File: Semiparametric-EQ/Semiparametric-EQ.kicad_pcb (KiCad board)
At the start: 2 copper layers, 100 x 100 mm, 52 parts, among them J1 Conn_01x05_Male, J2 Conn_01x02_Male, SW1 Peak/Shelf, U1 NE5532, U2 TL072, U3 NE5532

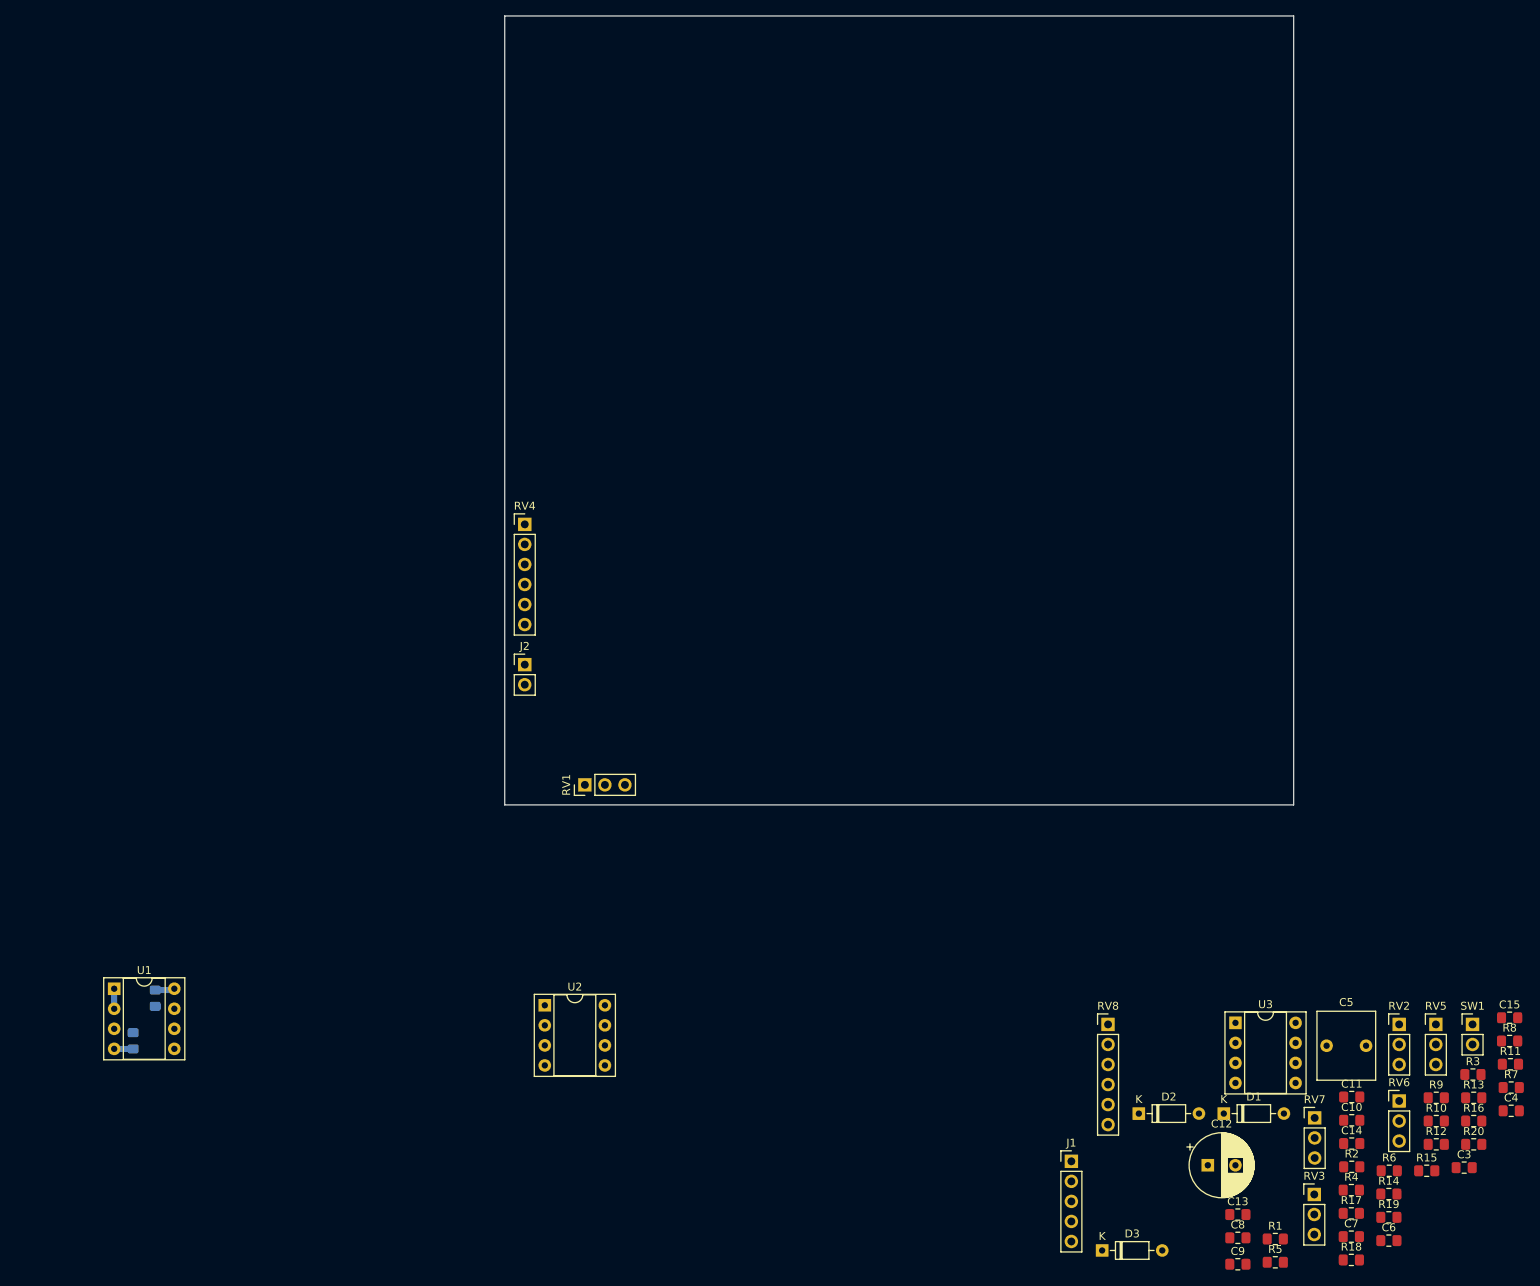
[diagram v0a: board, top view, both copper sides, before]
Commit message: More layout work on the EQ unit
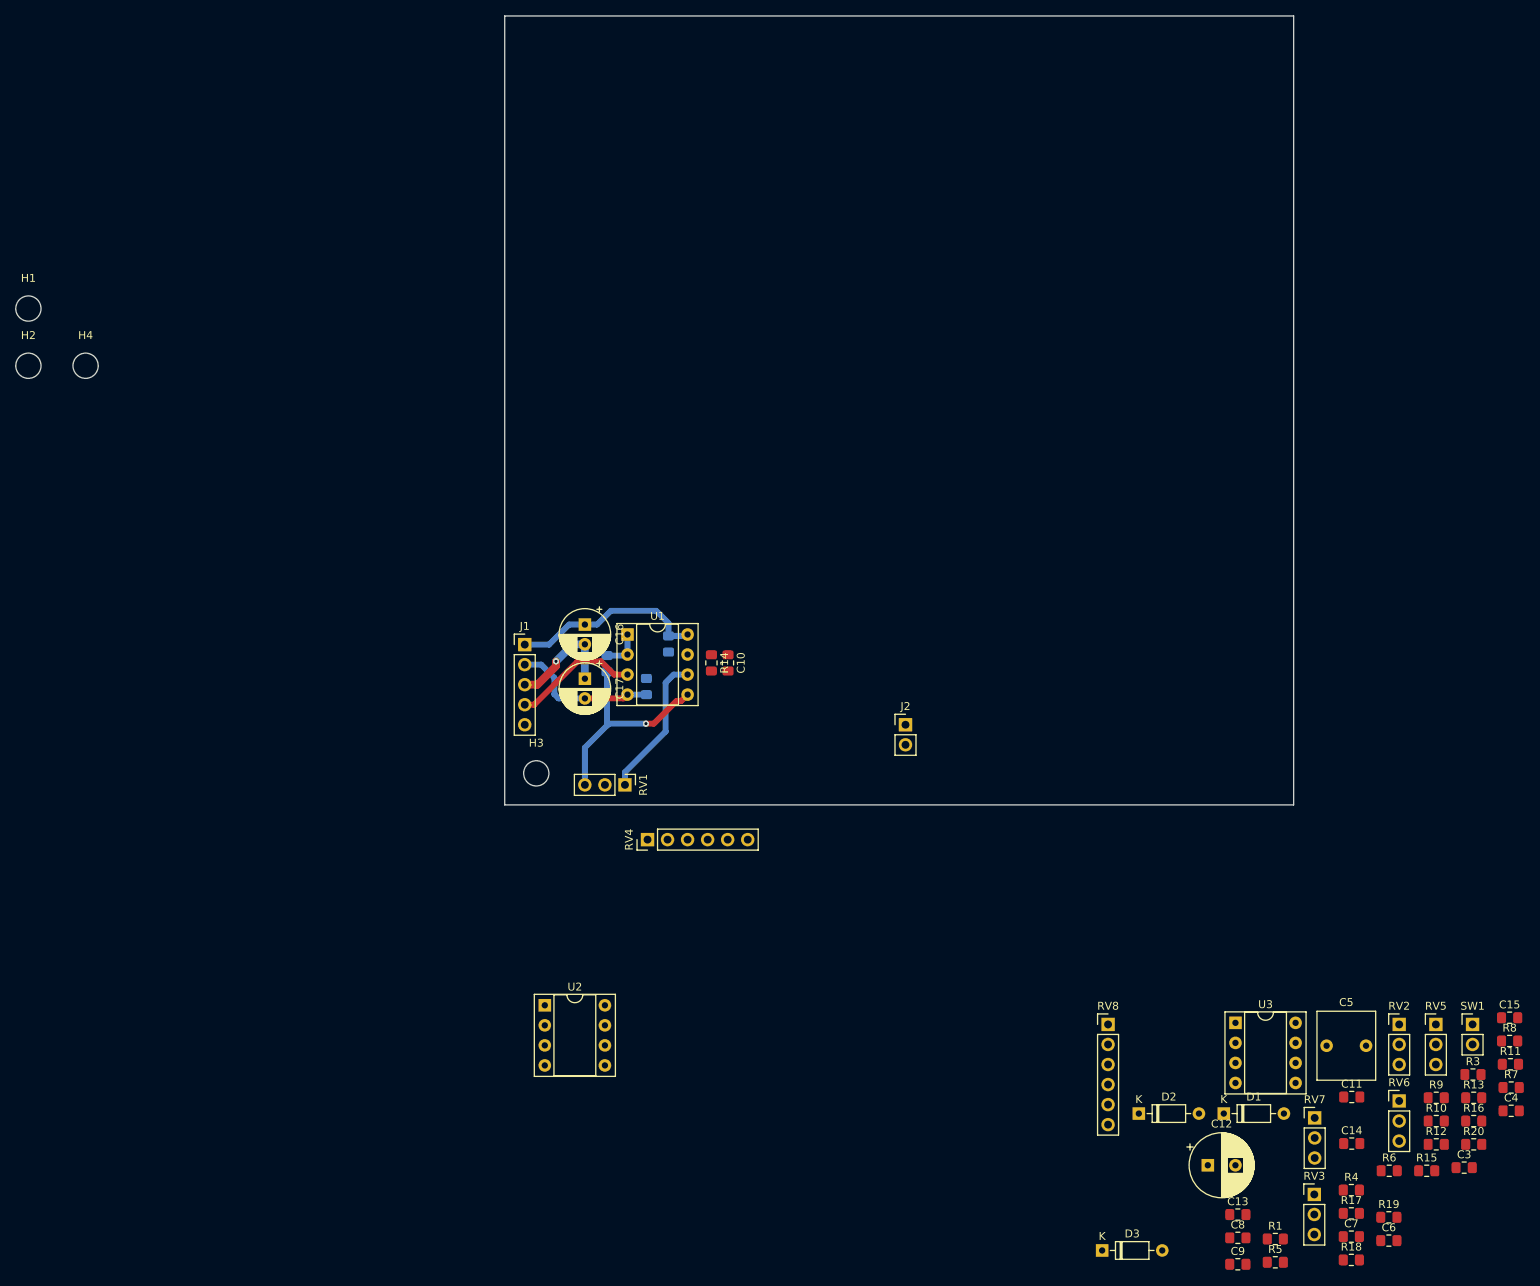
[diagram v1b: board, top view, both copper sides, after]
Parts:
- added C16: 100uF 25V, Capacitor_THT:CP_Radial_D6.3mm_P2.50mm, F.Cu at (10.2, -22.9)
- added C17: 100uF 25V, Capacitor_THT:CP_Radial_D6.3mm_P2.50mm, F.Cu at (10.2, -16.0)
- added H1: MountingHole, MountingHole:MountingHole_3.2mm_M3_ISO7380, F.Cu at (-60.4, -62.9)
- added H2: MountingHole, MountingHole:MountingHole_3.2mm_M3_ISO7380, F.Cu at (-60.4, -55.7)
- added H3: MountingHole, MountingHole:MountingHole_3.2mm_M3_ISO7380, F.Cu at (4.00, -4.00)
- added H4: MountingHole, MountingHole:MountingHole_3.2mm_M3_ISO7380, F.Cu at (-53.1, -55.7)
- R2: moved to B.Cu
- moved R2 113.9 mm to (13.0, -17.9), turned to 90 degrees
- moved R14 109.1 mm to (26.2, -18.0), turned to 270 degrees
- moved C10 98.0 mm to (28.3, -18.0), turned to 270 degrees
- moved J1 95.3 mm to (2.54, -20.3)
- moved C1 79.0 mm to (20.8, -20.4)
- moved C2 79.0 mm to (18.0, -15.0)
- moved U1 79.0 mm to (15.6, -21.6)
- moved J2 48.9 mm to (50.8, -10.2)
- moved RV4 42.9 mm to (18.1, 4.40), turned to 90 degrees
- moved RV1 5.08 mm to (15.2, -2.54), turned to 270 degrees
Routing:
- net Net-(R2-Pad1): track 0.00 -> 27.3 mm, vias 0 -> 1
- net +12V: track 2.49 -> 24.7 mm
- net Net-(C10-Pad2): track 0.00 -> 18.3 mm
- net -12V: track 2.40 -> 18.6 mm
- net IntoEQ: track 0.00 -> 16.0 mm
- net GND: track 0.00 -> 14.5 mm, vias 0 -> 1
- net Net-(R2-Pad2): track 2.54 -> 5.20 mm

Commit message: More layout on EQ
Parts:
- C10, C13, C14, C15, C7, C8, R1, R17, R5, R6: moved to B.Cu
- moved R4 139.9 mm to (-20.7, -7.60)
- moved C12 137.2 mm to (-8.40, -50.8)
- moved H1 125.5 mm to (61.0, -31.0)
- moved H4 125.3 mm to (61.0, -4.00)
- moved R1 124.0 mm to (4.30, -26.5), turned to 180 degrees
- moved C15 115.7 mm to (24.4, -25.8), turned to 270 degrees
- moved C14 108.9 mm to (27.7, -31.3), turned to 270 degrees
- moved RV2 107.6 mm to (10.2, -2.54), turned to 90 degrees
- moved SW1 107.5 mm to (20.3, -5.08)
- moved R8 100.4 mm to (36.9, -13.5)
- moved C7 98.1 mm to (29.7, -5.20)
- moved C5 97.5 mm to (17.7, -14.6), turned to 180 degrees
- moved R5 95.7 mm to (25.8, -5.20), turned to 180 degrees
- moved U3 92.5 mm to (22.2, -32.4)
- moved RV3 90.9 mm to (27.9, -2.54), turned to 90 degrees
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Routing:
- net Net-(C5-Pad2): track 0.00 -> 17.9 mm
- net GND: track 14.5 -> 0.00 mm, vias 1 -> 0
- net Net-(C10-Pad2): track 18.3 -> 30.3 mm
- net Net-(C5-Pad1): track 0.00 -> 10.6 mm
- net Net-(C8-Pad2): track 0.00 -> 7.63 mm
- net Net-(C13-Pad2): track 0.00 -> 7.59 mm
- net Net-(C10-Pad1): track 0.00 -> 5.47 mm
- net +12V: track 24.7 -> 30.0 mm
- net Net-(R17-Pad1): track 0.00 -> 5.09 mm
- net Net-(R6-Pad1): track 0.00 -> 4.33 mm
- net -12V: track 18.6 -> 14.9 mm
- net Net-(C7-Pad2): track 0.00 -> 2.76 mm
- net Net-(R5-Pad2): track 0.00 -> 2.45 mm
- net IntoEQ: track 16.0 -> 18.4 mm, vias 0 -> 1
- net Net-(C7-Pad1): track 0.00 -> 1.85 mm
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- added copper zone on B.Cu, net GND

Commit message: Finished first pass at Eq board
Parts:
- removed C3, C4: 0.1uF, Capacitor_SMD:C_0805_2012Metric_Pad1.15x1.40mm_HandSolder
- added C18: 0.1uF, Capacitor_SMD:C_0805_2012Metric_Pad1.15x1.40mm_HandSolder, B.Cu at (41.1, -22.5)
- added C19: 0.1uF, Capacitor_SMD:C_0805_2012Metric_Pad1.15x1.40mm_HandSolder, B.Cu at (33.7, -15.1)
- C10: moved to F.Cu
- C11, C6, C9, R10, R11, R16, R18, R19, R3, R7, R9: moved to B.Cu
- D1, D2, D3: footprint Diode_THT:D_DO-35_SOD27_P7.62mm_Horizontal -> Diode_SMD:D_SOD-123
- moved R7 120.3 mm to (19.9, -17.9), turned to 90 degrees
- moved C6 119.4 mm to (17.7, -17.9), turned to 270 degrees
- moved R3 108.7 mm to (26.2, -15.8), turned to 270 degrees
- moved R18 104.3 mm to (38.2, -20.4), turned to 90 degrees
- moved R9 102.1 mm to (33.2, -19.7), turned to 270 degrees
- moved R20 97.8 mm to (46.1, -17.7), turned to 270 degrees
- moved R19 96.2 mm to (46.1, -17.7), turned to 90 degrees
- moved D3 94.4 mm to (41.4, -31.5), turned to 270 degrees
- moved R11 94.1 mm to (52.9, -24.5), turned to 90 degrees
- moved R16 90.0 mm to (44.9, -5.00), turned to 180 degrees
- moved R15 89.9 mm to (55.7, -19.5), turned to 270 degrees
- moved R10 89.9 mm to (39.0, -2.60), turned to 180 degrees
- moved C9 88.2 mm to (53.7, -20.8)
- moved D1 87.9 mm to (38.8, -31.5), turned to 270 degrees
- moved R13 86.1 mm to (58.0, -19.5), turned to 270 degrees
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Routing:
- net FromEq: track 0.00 -> 94.3 mm
- net Net-(D1-Pad2): track 0.00 -> 77.1 mm, vias 0 -> 1
- net +12V: track 30.0 -> 100.1 mm
- net -12V: track 14.9 -> 70.8 mm, vias 0 -> 2
- net Net-(R2-Pad1): track 29.0 -> 76.0 mm, vias 1 -> 3
- net Net-(C10-Pad2): track 30.3 -> 76.8 mm, vias 0 -> 1
- net Net-(R7-Pad2): track 0.00 -> 44.1 mm, vias 0 -> 1
- net Net-(C6-Pad1): track 0.00 -> 37.2 mm, vias 0 -> 2
- net Para: track 0.00 -> 28.1 mm
- net Net-(R4-Pad2): track 0.00 -> 22.8 mm
- net Net-(R10-Pad2): track 0.00 -> 21.7 mm, vias 0 -> 1
- net Net-(C10-Pad1): track 5.47 -> 22.6 mm
- net Net-(C9-Pad2): track 0.00 -> 13.7 mm
- net Net-(R18-Pad1): track 0.00 -> 12.5 mm
- net Overload: track 0.00 -> 11.5 mm
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
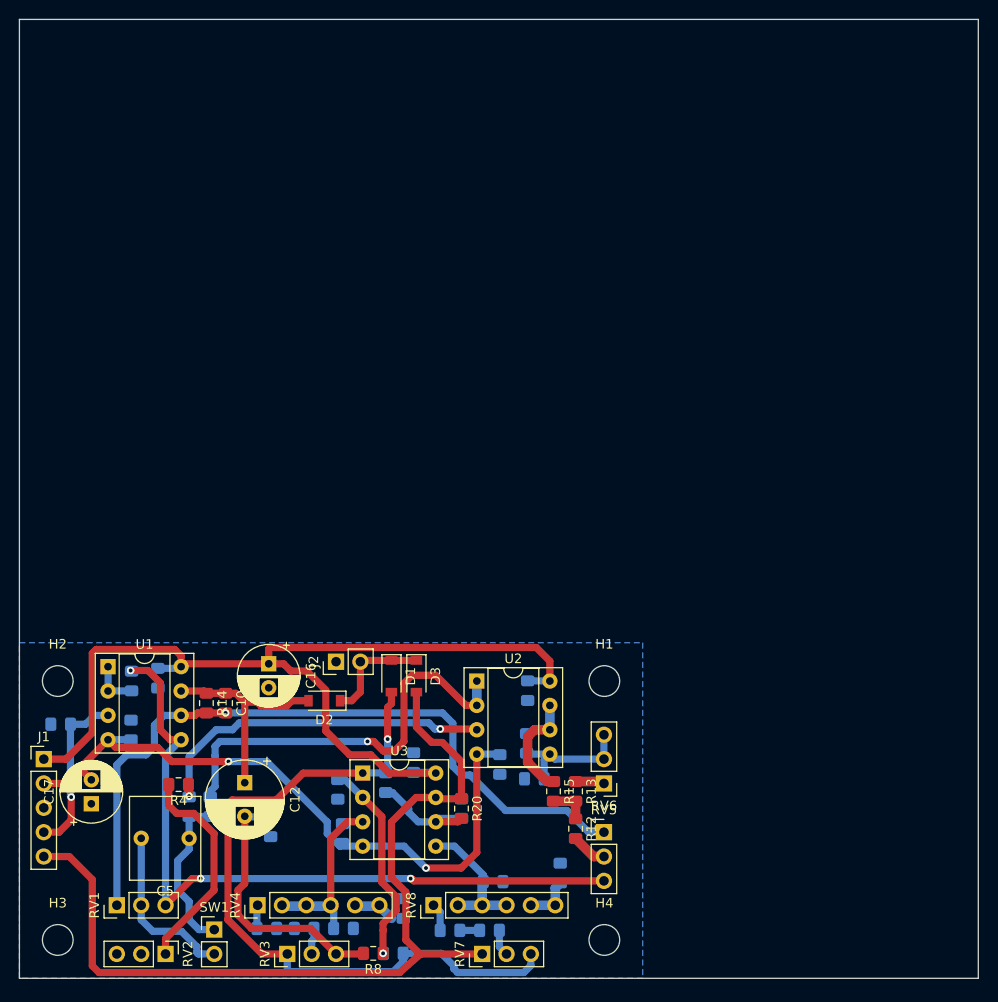
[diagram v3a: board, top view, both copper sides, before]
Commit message: Added top-side ground plane, started power supply work
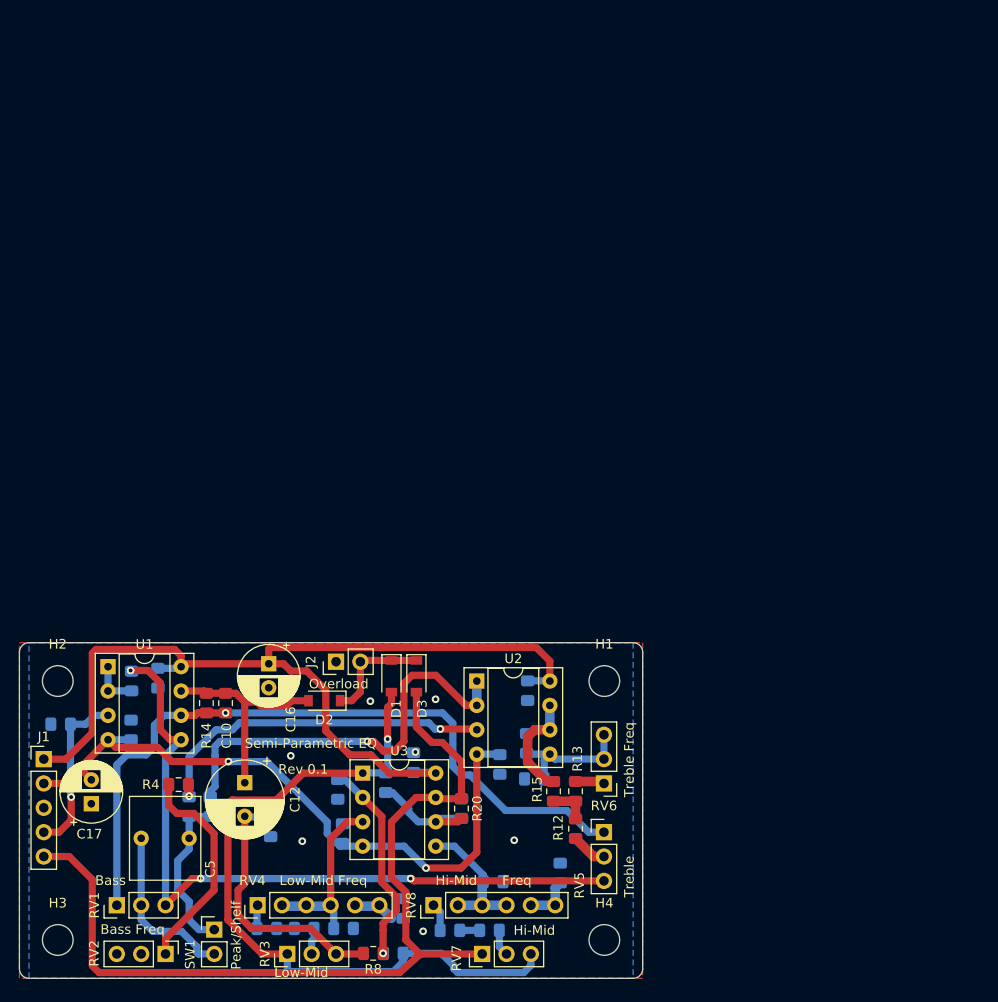
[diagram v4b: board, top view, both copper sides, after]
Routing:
- net GND: vias 0 -> 7
- added copper zone on F.Cu, net GND
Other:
- board size 100 x 100 mm -> 65 x 35 mm
- board text added: "Bass"
- board text added: "Bass Freq"
- board text added: "Hi-Mid"
- board text added: "Hi-Mid Freq"
- board text added: "Low-Mid"
- board text added: "Low-Mid Freq"
- board text added: "Overload"
- board text added: "Peak/Shelf"
- board text added: "Rev 0.1"
- board text added: "Semi-Parametric EQ"
- board text added: "Treble"
- board text added: "Treble Freq"
